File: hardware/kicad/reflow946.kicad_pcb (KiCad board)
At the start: 2 copper layers, 104 x 60 mm, 56 parts, among them J1 VH-2A, J2 VH-3A2, J3 VH-3A2, J4 XH-A2, J5 HDR-M-2.54_2x3, Q1 BTA16-600BRG, Q2 MMBT3906, Q3 MMBT3906, Q4 MMBT3906, SW1 SW_Push, SW2 SW_Push, SW3 SW_Push, U1 MOC3041M, U2 ESP32-WROOM-32U, U3 MAX31855KASA, U4 AMS1117-3.3

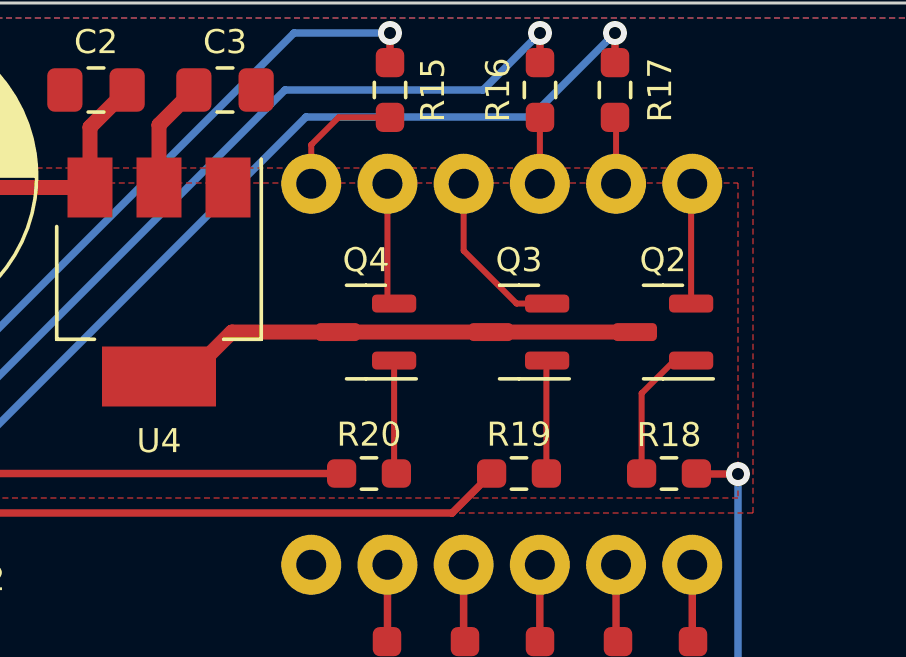
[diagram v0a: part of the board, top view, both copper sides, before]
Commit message: Fix PNP transistors missplacement
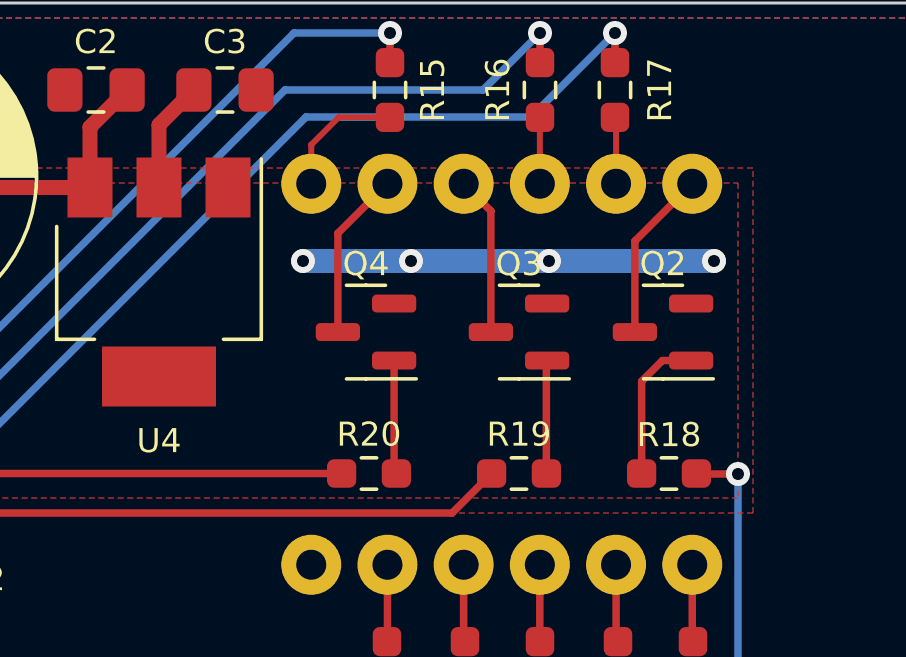
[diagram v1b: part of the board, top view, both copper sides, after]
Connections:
- Q2 pad 2: Net-(DS1-Pad12) -> +3.3V
- Q2 pad 3: +3.3V -> Net-(DS1-Pad12)
- Q3 pad 2: Net-(DS1-Pad9) -> +3.3V
- Q3 pad 3: +3.3V -> Net-(DS1-Pad9)
- Q4 pad 2: Net-(DS1-Pad8) -> +3.3V
- Q4 pad 3: +3.3V -> Net-(DS1-Pad8)
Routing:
- net +3.3V: track 144.0 -> 142.2 mm, vias 4 -> 8
- net Net-(DS1-Pad12): track 4.01 -> 5.74 mm
- net Net-(DS1-Pad8): track 4.09 -> 5.63 mm
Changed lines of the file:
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@@
     (property "Sheetname" "")
     (attr smd)
-    (fp_text reference "Q3" (at 0 2.4) (layer "F.SilkS")
+    (fp_text reference "Q3" (at 0 2.268344 180) (layer "F.SilkS")
       (effects (font (size 0.8 0.8) (thickness 0.15)))
     )
@@
       (net 36 "Net-(Q3-Pad1)") (pinfunction "B") (pintype "input"))
     (pad "2" smd roundrect (at -0.9375 0.95 180) (size 1.475 0.6) (layers "F.Cu" "F.Paste" "F.Mask") (roundrect_rratio 0.25)
-      (net 19 "Net-(DS1-Pad9)") (pinfunction "E") (pintype "passive"))
+      (net 16 "+3.3V") (pinfunction "E") (pintype "passive"))
     (pad "3" smd roundrect (at 0.9375 0 180) (size 1.475 0.6) (layers "F.Cu" "F.Paste" "F.Mask") (roundrect_rratio 0.25)
-      (net 16 "+3.3V") (pinfunction "C") (pintype "passive"))
+      (net 19 "Net-(DS1-Pad9)") (pinfunction "C") (pintype "passive"))
     (model "${KICAD6_3DMODEL_DIR}/Package_TO_SOT_SMD.3dshapes/SOT-23.wrl"
       (offset (xyz 0 0 0))
@@
     (property "Sheetname" "")
     (attr smd)
-    (fp_text reference "Q4" (at 0 2.4) (layer "F.SilkS")
+    (fp_text reference "Q4" (at 0 2.268344 180) (layer "F.SilkS")
       (effects (font (size 0.8 0.8) (thickness 0.15)))
     )
@@
       (net 37 "Net-(Q4-Pad1)") (pinfunction "B") (pintype "input"))
     (pad "2" smd roundrect (at -0.9375 0.95 180) (size 1.475 0.6) (layers "F.Cu" "F.Paste" "F.Mask") (roundrect_rratio 0.25)
-      (net 18 "Net-(DS1-Pad8)") (pinfunction "E") (pintype "passive"))
+      (net 16 "+3.3V") (pinfunction "E") (pintype "passive"))
     (pad "3" smd roundrect (at 0.9375 0 180) (size 1.475 0.6) (layers "F.Cu" "F.Paste" "F.Mask") (roundrect_rratio 0.25)
-      (net 16 "+3.3V") (pinfunction "C") (pintype "passive"))
+      (net 18 "Net-(DS1-Pad8)") (pinfunction "C") (pintype "passive"))
     (model "${KICAD6_3DMODEL_DIR}/Package_TO_SOT_SMD.3dshapes/SOT-23.wrl"
       (offset (xyz 0 0 0))
@@
     (property "Sheetname" "")
     (attr smd)
-    (fp_text reference "Q2" (at 0 2.4) (layer "F.SilkS")
+    (fp_text reference "Q2" (at 0 2.268344 180) (layer "F.SilkS")
       (effects (font (size 0.8 0.8) (thickness 0.15)))
     )
@@
       (net 35 "Net-(Q2-Pad1)") (pinfunction "B") (pintype "input"))
     (pad "2" smd roundrect (at -0.9375 0.95 180) (size 1.475 0.6) (layers "F.Cu" "F.Paste" "F.Mask") (roundrect_rratio 0.25)
-      (net 24 "Net-(DS1-Pad12)") (pinfunction "E") (pintype "passive"))
+      (net 16 "+3.3V") (pinfunction "E") (pintype "passive"))
     (pad "3" smd roundrect (at 0.9375 0 180) (size 1.475 0.6) (layers "F.Cu" "F.Paste" "F.Mask") (roundrect_rratio 0.25)
-      (net 16 "+3.3V") (pinfunction "C") (pintype "passive"))
+      (net 24 "Net-(DS1-Pad12)") (pinfunction "C") (pintype "passive"))
     (model "${KICAD6_3DMODEL_DIR}/Package_TO_SOT_SMD.3dshapes/SOT-23.wrl"
       (offset (xyz 0 0 0))
@@
   (segment (start 112.525 120.9) (end 109 120.9) (width 0.5) (layer "F.Cu") (net 16))
   (segment (start 109.015 108.3) (end 109.015 106.715) (width 1) (layer "F.Cu") (net 16))
-  (segment (start 133.631656 80.968344) (end 132.15 82.45) (width 0.5) (layer "F.Cu") (net 16))
   (segment (start 112.525 120.9) (end 112.525 119.405) (width 0.5) (layer "F.Cu") (net 16))
   (segment (start 132.15 82.45) (end 131.2 82.45) (width 0.5) (layer "F.Cu") (net 16))
   (segment (start 109.015 109.485) (end 109.015 108.3) (width 0.5) (layer "F.Cu") (net 16))
   (segment (start 109.015 106.715) (end 109 106.7) (width 1) (layer "F.Cu") (net 16))
-  (segment (start 142.2625 80.968344) (end 147.0625 80.968344) (width 0.5) (layer "F.Cu") (net 16))
   (segment (start 107.7 110.8) (end 107.7 110.6625) (width 0.5) (layer "F.Cu") (net 16))
-  (segment (start 137.1625 80.968344) (end 142.2625 80.968344) (width 0.5) (layer "F.Cu") (net 16))
   (segment (start 131.2 74.0625) (end 132.3625 72.9) (width 0.5) (layer "F.Cu") (net 16))
   (segment (start 107.8375 110.6625) (end 109.015 109.485) (width 0.5) (layer "F.Cu") (net 16))
@@
   (segment (start 138.5 120.9125) (end 127.5 120.9125) (width 0.5) (layer "F.Cu") (net 16))
   (segment (start 131.2 76.15) (end 131.2 74.0625) (width 0.5) (layer "F.Cu") (net 16))
-  (segment (start 137.1625 80.968344) (end 133.631656 80.968344) (width 0.5) (layer "F.Cu") (net 16))
   (segment (start 110.3 112.8125) (end 109.7125 112.8125) (width 0.5) (layer "F.Cu") (net 16))
   (segment (start 154.5 120.9125) (end 138.5 120.9125) (width 0.5) (layer "F.Cu") (net 16))
   (via (at 124.2 79.5) (size 0.8) (drill 0.4) (layers "F.Cu" "B.Cu") (net 16))
+  (via (at 144.2 78.6) (size 0.8) (drill 0.4) (layers "F.Cu" "B.Cu") (free) (net 16))
   (via (at 109 106.7) (size 0.8) (drill 0.4) (layers "F.Cu" "B.Cu") (net 16))
   (via (at 109 120.9) (size 0.8) (drill 0.4) (layers "F.Cu" "B.Cu") (net 16))
+  (via (at 139.6 78.6) (size 0.8) (drill 0.4) (layers "F.Cu" "B.Cu") (free) (net 16))
   (via (at 124.2 81) (size 0.8) (drill 0.4) (layers "F.Cu" "B.Cu") (net 16))
+  (via (at 149.7 78.6) (size 0.8) (drill 0.4) (layers "F.Cu" "B.Cu") (free) (net 16))
+  (via (at 136 78.6) (size 0.8) (drill 0.4) (layers "F.Cu" "B.Cu") (free) (net 16))
   (segment (start 124.2 81) (end 124.2 79.5) (width 1) (layer "B.Cu") (net 16))
   (segment (start 107.465 71.535) (end 108.675 71.535) (width 1) (layer "B.Cu") (net 16))
+  (segment (start 149.7 78.6) (end 144.2 78.6) (width 0.8) (layer "B.Cu") (net 16))
   (segment (start 109 81) (end 124.2 81) (width 1) (layer "B.Cu") (net 16))
   (segment (start 109 85.9) (end 109 77.5) (width 1) (layer "B.Cu") (net 16))
   (segment (start 109 77.5) (end 106.6 75.1) (width 1) (layer "B.Cu") (net 16))
   (segment (start 106.6 72.4) (end 107.465 71.535) (width 1) (layer "B.Cu") (net 16))
+  (segment (start 139.6 78.6) (end 144.2 78.6) (width 0.8) (layer "B.Cu") (net 16))
+  (segment (start 136 78.6) (end 139.6 78.6) (width 0.8) (layer "B.Cu") (net 16))
   (segment (start 109 106.7) (end 109 120.9) (width 1) (layer "B.Cu") (net 16))
   (segment (start 106.6 75.1) (end 106.6 72.4) (width 1) (layer "B.Cu") (net 16))
@@
   (segment (start 136.275 74.725) (end 137.1875 73.8125) (width 0.2) (layer "F.Cu") (net 17))
   (segment (start 137.1875 73.8125) (end 138.9 73.8125) (width 0.2) (layer "F.Cu") (net 17))
-  (segment (start 138.815 76.02513) (end 138.815 79.795844) (width 0.2) (layer "F.Cu") (net 18))
-  (segment (start 138.815 79.795844) (end 139.0375 80.018344) (width 0.2) (layer "F.Cu") (net 18))
-  (segment (start 141.355 78.255) (end 143.118344 80.018344) (width 0.2) (layer "F.Cu") (net 19))
-  (segment (start 143.118344 80.018344) (end 144.1375 80.018344) (width 0.2) (layer "F.Cu") (net 19))
-  (segment (start 141.355 76.02513) (end 141.355 78.255) (width 0.2) (layer "F.Cu") (net 19))
+  (segment (start 137.1625 77.67763) (end 138.815 76.02513) (width 0.25) (layer "F.Cu") (net 18))
+  (segment (start 137.1625 80.968344) (end 137.1625 77.67763) (width 0.25) (layer "F.Cu") (net 18))
+  (segment (start 142.2625 76.93263) (end 141.355 76.02513) (width 0.25) (layer "F.Cu") (net 19))
+  (segment (start 142.2625 80.968344) (end 142.2625 76.93263) (width 0.25) (layer "F.Cu") (net 19))
   (segment (start 112.725 80) (end 112.7 80.025) (width 0.5) (layer "F.Cu") (net 20))
   (segment (start 112.7 80.025) (end 112.7 82.15) (width 0.5) (layer "F.Cu") (net 20))
@@
   (segment (start 146.435 76.02513) (end 146.435 73.8475) (width 0.2) (layer "F.Cu") (net 23))
   (segment (start 146.435 73.8475) (end 146.4 73.8125) (width 0.2) (layer "F.Cu") (net 23))
-  (segment (start 148.9375 80.018344) (end 148.9375 76.06263) (width 0.2) (layer "F.Cu") (net 24))
-  (segment (start 148.9375 76.06263) (end 148.975 76.02513) (width 0.2) (layer "F.Cu") (net 24))
+  (segment (start 147.0625 80.968344) (end 147.0625 77.93763) (width 0.25) (layer "F.Cu") (net 24))
+  (segment (start 147.0625 77.93763) (end 148.975 76.02513) (width 0.25) (layer "F.Cu") (net 24))
   (segment (start 120.1 110.8875) (end 120.1 111.8) (width 0.25) (layer "F.Cu") (net 25))
   (segment (start 119.8125 110.6) (end 120.1 110.8875) (width 0.25) (layer "F.Cu") (net 25))
@@
   (via (at 117.187702 86.3877) (size 0.8) (drill 0.4) (layers "F.Cu" "B.Cu") (net 31))
   (segment (start 119.2 88.4) (end 117.187702 86.3877) (width 0.25) (layer "B.Cu") (net 31))
-  (segment (start 148.381656 81.918344) (end 148.9375 81.918344) (width 0.2) (layer "F.Cu") (net 35))
-  (segment (start 147.2875 83.0125) (end 148.381656 81.918344) (width 0.2) (layer "F.Cu") (net 35))
-  (segment (start 147.2875 85.683858) (end 147.2875 83.0125) (width 0.2) (layer "F.Cu") (net 35))
-  (segment (start 144.1125 81.943344) (end 144.1375 81.918344) (width 0.2) (layer "F.Cu") (net 36))
-  (segment (start 144.1125 85.683858) (end 144.1125 81.943344) (width 0.2) (layer "F.Cu") (net 36))
-  (segment (start 139.1125 85.683858) (end 139.0375 85.608858) (width 0.2) (layer "F.Cu") (net 37))
-  (segment (start 139.0375 85.608858) (end 139.0375 81.918344) (width 0.2) (layer "F.Cu") (net 37))
+  (segment (start 147.2875 82.6125) (end 147.2875 85.683858) (width 0.25) (layer "F.Cu") (net 35))
+  (segment (start 148.9375 81.918344) (end 147.981656 81.918344) (width 0.25) (layer "F.Cu") (net 35))
+  (segment (start 147.981656 81.918344) (end 147.2875 82.6125) (width 0.25) (layer "F.Cu") (net 35))
+  (segment (start 144.1375 81.918344) (end 144.1125 81.943344) (width 0.25) (layer "F.Cu") (net 36))
+  (segment (start 144.1125 81.943344) (end 144.1125 85.683858) (width 0.25) (layer "F.Cu") (net 36))
+  (segment (start 139.0375 81.918344) (end 139.0375 85.608858) (width 0.25) (layer "F.Cu") (net 37))
+  (segment (start 139.0375 85.608858) (end 139.1125 85.683858) (width 0.25) (layer "F.Cu") (net 37))
   (segment (start 117.905 110.5175) (end 117.9875 110.6) (width 0.25) (layer "F.Cu") (net 38))
   (segment (start 117.905 108.3) (end 117.905 110.5175) (width 0.25) (layer "F.Cu") (net 38))
